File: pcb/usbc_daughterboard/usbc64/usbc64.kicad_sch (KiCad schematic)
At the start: 11 parts, among them J1 USB_C_Receptacle_USB2.0, J2 Conn_01x04, U1 ESDALD05UG4

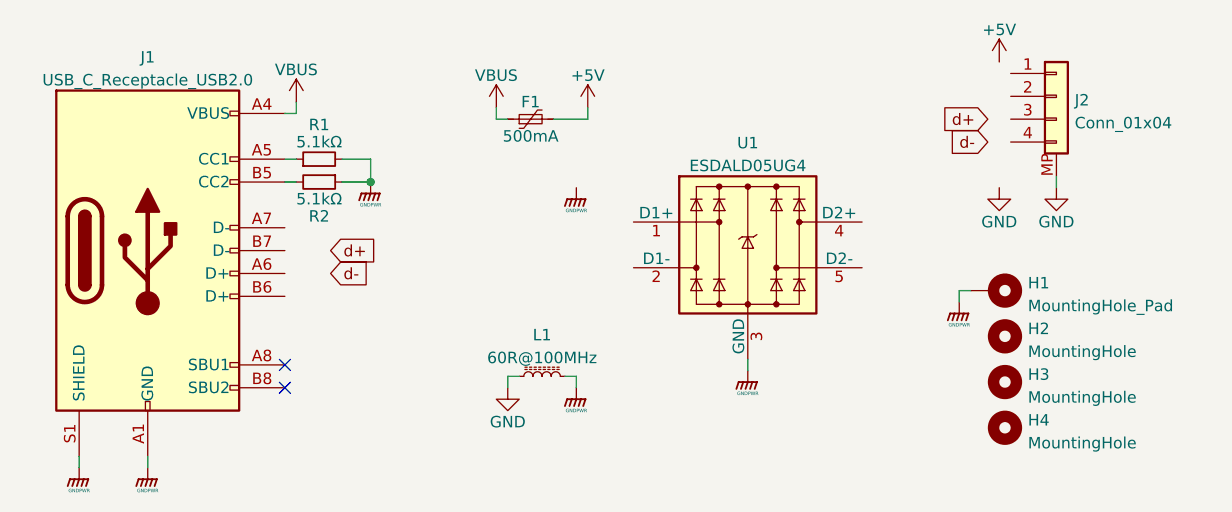
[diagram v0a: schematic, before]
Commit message: esdald05ug4 symbol
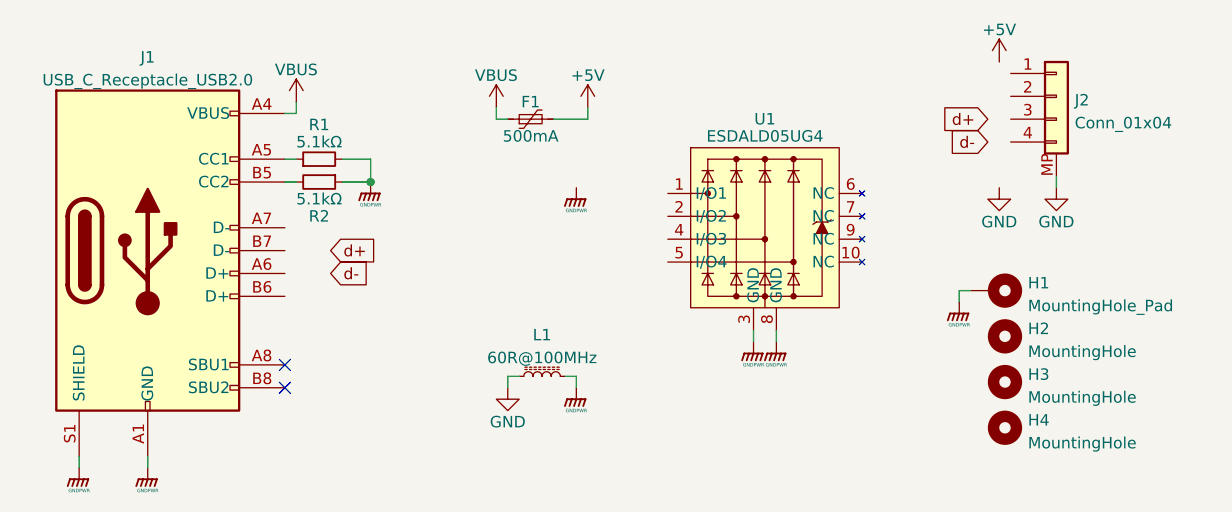
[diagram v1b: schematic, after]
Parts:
- U1: symbol Power_Protection:TPD4EUSB30 -> ESDALD05UG4:ESDALD05UG4
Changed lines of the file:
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@@
+    (stroke (width 0) (type default) (color 0 0 0 0))
+  )
+  (wire (pts (xy 118.745 66.675) (xy 118.745 67.945))
     (stroke (width 0) (type default) (color 0 0 0 0))
   )
@@
     (stroke (width 0) (type default) (color 0 0 0 0))
   )
-  (wire (pts (xy 115.57 69.85) (xy 115.57 71.12))
+  (wire (pts (xy 116.205 66.675) (xy 116.205 67.945))
     (stroke (width 0) (type default) (color 0 0 0 0))
   )
@@
     (pin "1")
   )
-  (symbol (lib_id "Power_Protection:TPD4EUSB30") (at 115.57 57.15 0) (unit 1)
-    (in_bom yes) (on_board yes) (fields_autoplaced)
-    (property "Reference" "U1" (id 0) (at 115.57 45.8302 0))
-    (property "Value" "ESDALD05UG4" (id 1) (at 115.57 48.3671 0))
-    (property "Footprint" "Package_DFN_QFN:UDFN-10_1.35x2.6mm_P0.5mm" (id 2) (at 91.44 67.31 0)
-      (effects (font (size 1.27 1.27)) hide)
-    )
-    (property "Datasheet" "http://www.ti.com/lit/ds/symlink/tpd2eusb30a.pdf" (id 3) (at 115.57 57.15 0)
+  (symbol (lib_id "ESDALD05UG4:ESDALD05UG4") (at 117.475 55.245 0) (unit 1)
+    (in_bom yes) (on_board yes)
+    (property "Reference" "U1" (id 0) (at 117.475 43.18 0))
+    (property "Value" "ESDALD05UG4" (id 1) (at 117.475 45.085 0))
+    (property "Footprint" "Package_DFN_QFN:UDFN-10_1.35x2.6mm_P0.5mm" (id 2) (at 117.475 47.625 0)
+      (effects (font (size 1.27 1.27)) hide)
+    )
+    (property "Datasheet" "http://www.ti.com/lit/ds/symlink/tpd2eusb30a.pdf" (id 3) (at 117.475 47.625 0)
       (effects (font (size 1.27 1.27)) hide)
     )
@@
     (pin "1")
   )
-  (symbol (lib_id "power:GNDPWR") (at 115.57 71.12 0) (unit 1)
-    (in_bom yes) (on_board yes)
-    (property "Reference" "#PWR0113" (id 0) (at 115.57 76.2 0)
-      (effects (font (size 1.27 1.27)) hide)
-    )
-    (property "Value" "GNDPWR" (id 1) (at 115.57 73.66 0)
-      (effects (font (size 0.381 0.381)))
-    )
-    (property "Footprint" "" (id 2) (at 115.57 72.39 0)
-      (effects (font (size 1.27 1.27)) hide)
-    )
-    (property "Datasheet" "" (id 3) (at 115.57 72.39 0)
+  (symbol (lib_id "power:GNDPWR") (at 118.745 67.945 0) (unit 1)
+    (in_bom yes) (on_board yes)
+    (property "Reference" "#PWR?" (id 0) (at 118.745 73.025 0)
+      (effects (font (size 1.27 1.27)) hide)
+    )
+    (property "Value" "GNDPWR" (id 1) (at 118.745 70.485 0)
+      (effects (font (size 0.381 0.381)))
+    )
+    (property "Footprint" "" (id 2) (at 118.745 69.215 0)
+      (effects (font (size 1.27 1.27)) hide)
+    )
+    (property "Datasheet" "" (id 3) (at 118.745 69.215 0)
+      (effects (font (size 1.27 1.27)) hide)
+    )
+    (pin "1")
+  )
+  (symbol (lib_id "power:GNDPWR") (at 116.205 67.945 0) (unit 1)
+    (in_bom yes) (on_board yes)
+    (property "Reference" "#PWR0113" (id 0) (at 116.205 73.025 0)
+      (effects (font (size 1.27 1.27)) hide)
+    )
+    (property "Value" "GNDPWR" (id 1) (at 116.205 70.485 0)
+      (effects (font (size 0.381 0.381)))
+    )
+    (property "Footprint" "" (id 2) (at 116.205 69.215 0)
+      (effects (font (size 1.27 1.27)) hide)
+    )
+    (property "Datasheet" "" (id 3) (at 116.205 69.215 0)
       (effects (font (size 1.27 1.27)) hide)
     )
@@
       (reference "#PWR0114") (unit 1) (value "GNDPWR") (footprint "")
     )
+    (path "/da5d9f7d-1132-4948-a5d2-b2184eb71b56"
+      (reference "#PWR?") (unit 1) (value "GNDPWR") (footprint "")
+    )
     (path "/062791e6-12f0-44fc-90f6-45f64ecdec87"
